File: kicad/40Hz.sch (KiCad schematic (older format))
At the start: 30 parts, among them J1 Power, J2 5V, J3 SSD1306, Q1 IRF540N, SW1 CANC, SW2 UP, SW3 DOWN, SW4 ENT, U1 ESP-12F, U2 WeMos_D1_mini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

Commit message: UPD
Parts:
- SW1: value CANC -> OK
- SW4: value ENT -> CANC
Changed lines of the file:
@@
 P 2200 4950
 F 0 "SW1" H 2200 5235 50  0000 C CNN
-F 1 "CANC" H 2200 5144 50  0000 C CNN
+F 1 "OK" H 2200 5144 50  0000 C CNN
 F 2 "Button_Switch_THT:SW_PUSH_6mm_H5mm" H 2200 5150 50  0001 C CNN
 F 3 "~" H 2200 5150 50  0001 C CNN
@@
 P 2200 6350
 F 0 "SW4" H 2200 6635 50  0000 C CNN
-F 1 "ENT" H 2200 6544 50  0000 C CNN
+F 1 "CANC" H 2200 6544 50  0000 C CNN
 F 2 "Button_Switch_THT:SW_PUSH_6mm_H5mm" H 2200 6550 50  0001 C CNN
 F 3 "~" H 2200 6550 50  0001 C CNN
@@
 	2000 4950 1050 4950
 Text Label 1800 4950 0    50   ~ 0
-IO16
+IO14
 Text Label 1800 5900 0    50   ~ 0
 IO12
@@
 	1300 5400 1300 6400
 Text Label 1800 5400 0    50   ~ 0
-IO14
+IO16
 Wire Wire Line
 	1300 6750 1550 6750

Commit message: Schematics update
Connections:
- wire segments 136 -> 134
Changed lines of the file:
@@
 	1    0    0    -1
 $EndComp
-Wire Wire Line
-	5750 4850 5450 4850
-Wire Wire Line
-	5750 4950 5450 4950
-Text Label 5500 4850 0    50   ~ 0
-ACIN1
-Text Label 5500 4950 0    50   ~ 0
-ACIN2
 Text Label 8550 5350 0    50   ~ 0
 ACIN1

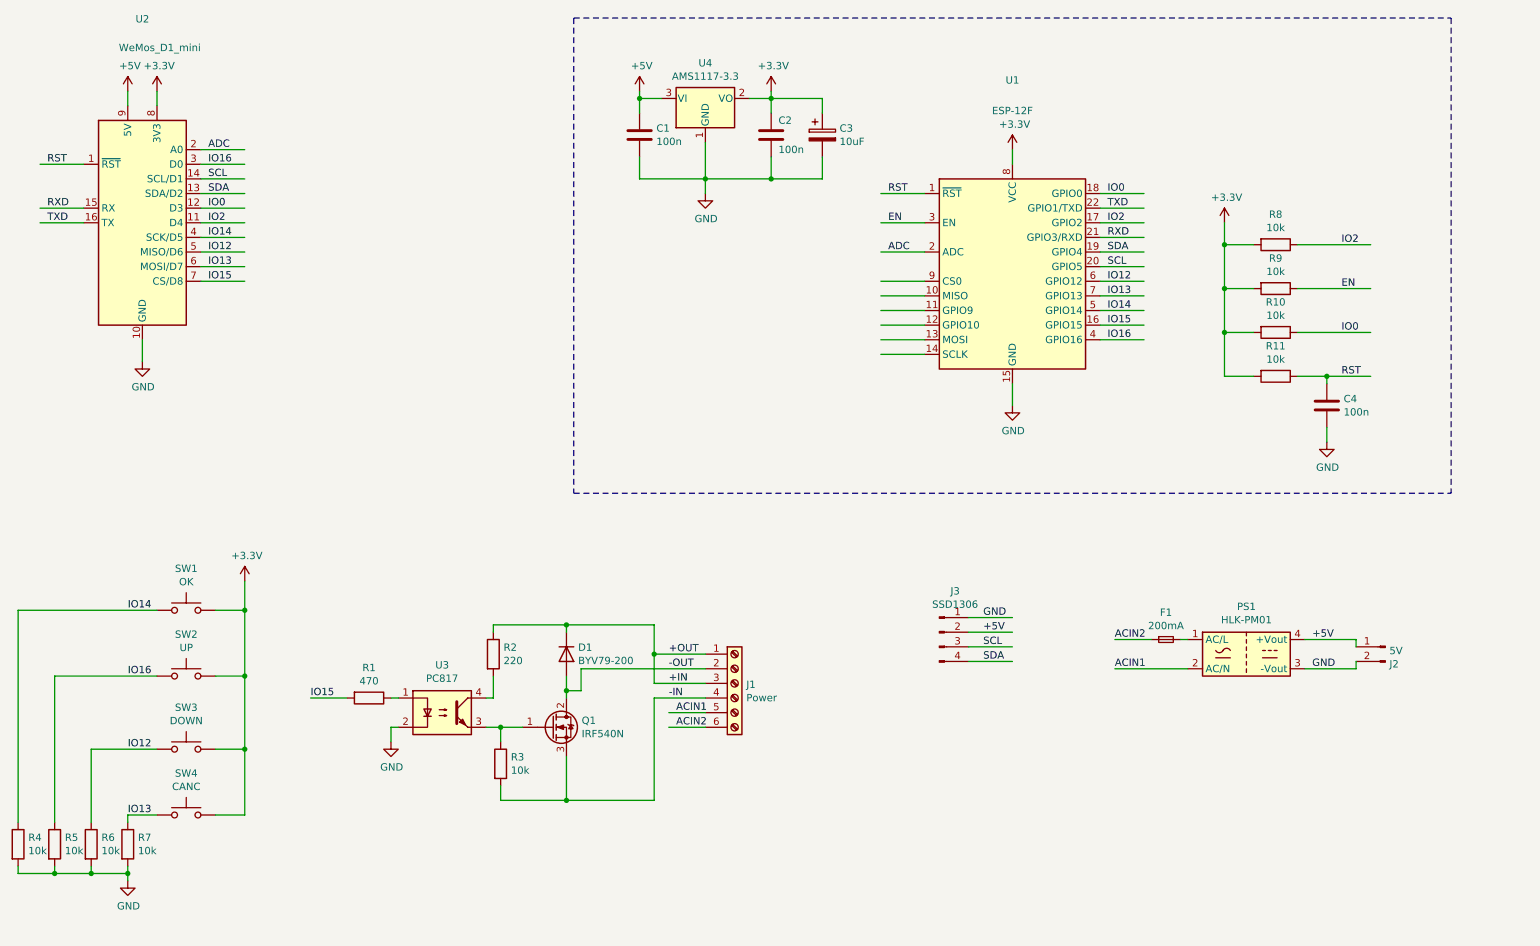
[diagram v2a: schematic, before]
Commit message: Add CRC Check on Settings
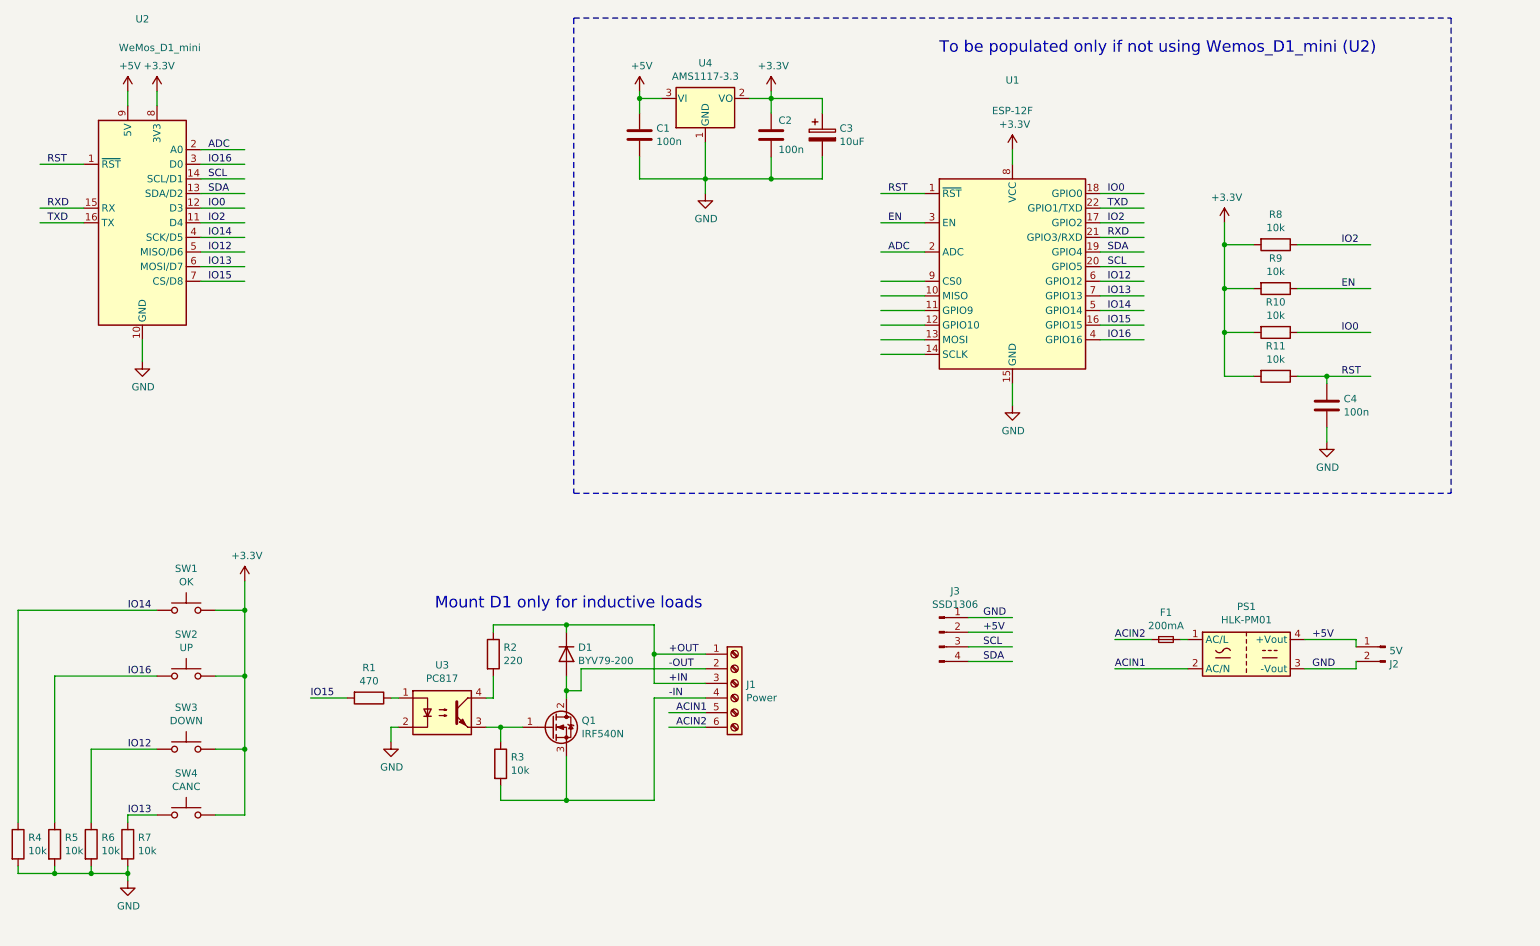
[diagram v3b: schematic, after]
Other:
- note added: "Mount D1 only for inductive loads"
- note added: "To be populated only if not using Wemos_D1_mini (U2)"
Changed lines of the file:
@@
 	4800 6250 4800 5950
 Connection ~ 4800 6250
-$Comp
-L Diode:BYV79-200 D1
-U 1 1 61F3A6D4
-P 4800 5250
-F 0 "D1" V 4754 5330 50  0000 L CNN
-F 1 "BYV79-200" V 4845 5330 50  0000 L CNN
-F 2 "Diode_THT:D_DO-15_P5.08mm_Vertical_KathodeUp" H 4800 5075 50  0001 C CNN
-F 3 "http://pdf.datasheetcatalog.com/datasheet/philips/BYV79-100.pdf" H 4800 5250 50  0001 C CNN
-	1    4800 5250
-	0    1    1    0
-$EndComp
 Connection ~ 4800 5050
 Wire Wire Line
@@
 Text Label 5550 5750 0    50   ~ 0
 ACIN2
+Text Notes 7350 1150 0    79   ~ 0
+To be populated only if not using Wemos_D1_mini (U2)
+$Comp
+L Diode:BYV79-200 D1
+U 1 1 61F3A6D4
+P 4800 5250
+F 0 "D1" V 4754 5330 50  0000 L CNN
+F 1 "BYV79-200" V 4845 5330 50  0000 L CNN
+F 2 "Diode_THT:D_DO-15_P5.08mm_Vertical_KathodeUp" H 4800 5075 50  0001 C CNN
+F 3 "http://pdf.datasheetcatalog.com/datasheet/philips/BYV79-100.pdf" H 4800 5250 50  0001 C CNN
+	1    4800 5250
+	0    1    1    0
+$EndComp
+Text Notes 3900 4950 0    79   ~ 0
+Mount D1 only for inductive loads
 $EndSCHEMATC

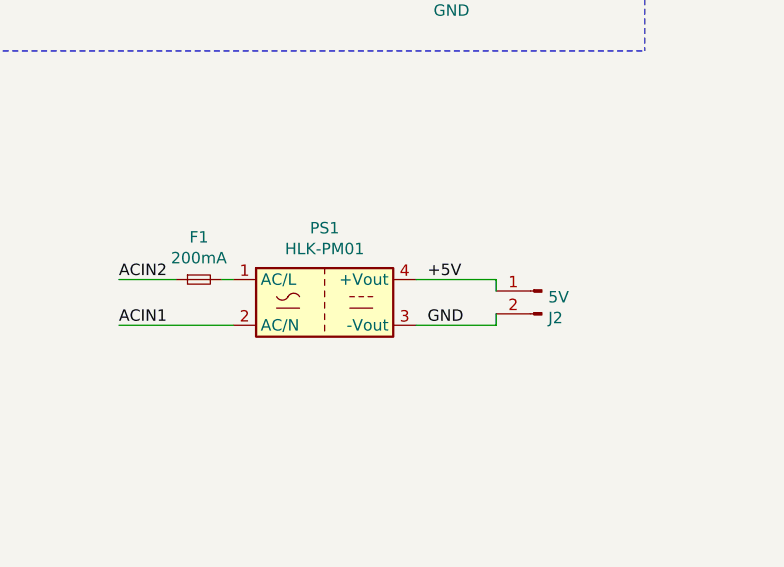
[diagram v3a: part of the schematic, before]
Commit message: Fuse added
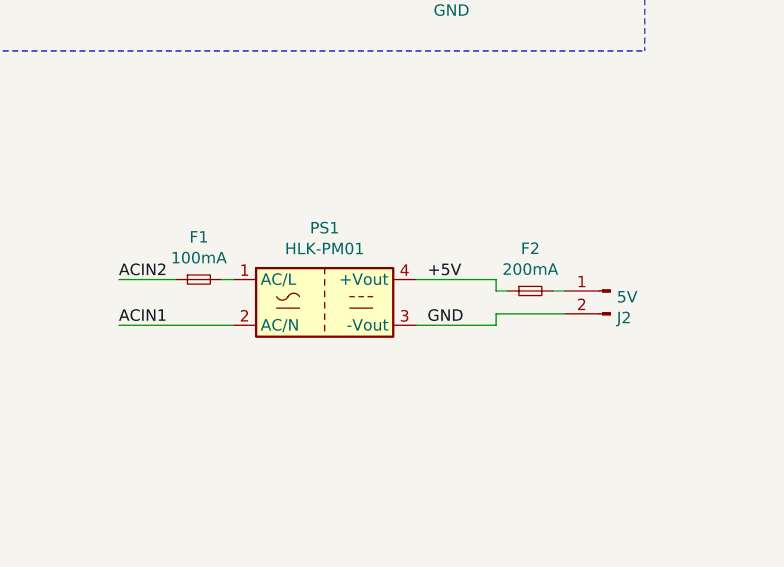
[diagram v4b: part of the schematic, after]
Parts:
- added F2: 200mA, Fuse:Fuse_1206_3216Metric, symbol Device:Fuse_Small
- F1: value 200mA -> 100mA
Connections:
- wire segments 134 -> 137
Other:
- moved on the sheet: J2
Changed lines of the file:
@@
 P 8900 5150
 F 0 "F1" H 8900 5335 50  0000 C CNN
-F 1 "200mA" H 8900 5244 50  0000 C CNN
+F 1 "100mA" H 8900 5244 50  0000 C CNN
 F 2 "Fuse:Fuse_1206_3216Metric" H 8900 5150 50  0001 C CNN
 F 3 "~" H 8900 5150 50  0001 C CNN
@@
 L Connector:Conn_01x02_Male J2
 U 1 1 622AC1D8
-P 10400 5200
-F 0 "J2" H 10372 5082 50  0000 R CNN
-F 1 "5V" H 10372 5173 50  0000 R CNN
-F 2 "TerminalBlock_Phoenix:TerminalBlock_Phoenix_MKDS-3-2-5.08_1x02_P5.08mm_Horizontal" H 10400 5200 50  0001 C CNN
-F 3 "~" H 10400 5200 50  0001 C CNN
-	1    10400 5200
+P 10700 5200
+F 0 "J2" H 10672 5082 50  0000 R CNN
+F 1 "5V" H 10672 5173 50  0000 R CNN
+F 2 "TerminalBlock_Phoenix:TerminalBlock_Phoenix_MKDS-3-2-5.08_1x02_P5.08mm_Horizontal" H 10700 5200 50  0001 C CNN
+F 3 "~" H 10700 5200 50  0001 C CNN
+	1    10700 5200
 	-1   0    0    -1
 $EndComp
@@
 Text Notes 3900 4950 0    79   ~ 0
 Mount D1 only for inductive loads
+$Comp
+L Device:Fuse_Small F2
+U 1 1 621A756A
+P 10350 5200
+F 0 "F2" H 10350 5385 50  0000 C CNN
+F 1 "200mA" H 10350 5294 50  0000 C CNN
+F 2 "Fuse:Fuse_1206_3216Metric" H 10350 5200 50  0001 C CNN
+F 3 "~" H 10350 5200 50  0001 C CNN
+	1    10350 5200
+	1    0    0    -1
+$EndComp
+Wire Wire Line
+	10200 5200 10250 5200
+Wire Wire Line
+	10500 5200 10450 5200
+Wire Wire Line
+	10500 5300 10200 5300
 $EndSCHEMATC

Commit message: Schematic update
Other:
- note added: "Optional AC Power Supply"
- moved on the sheet: F1, F2, J2, J3, PS1, U2
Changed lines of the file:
@@
 	7250 2100 6950 2100
 Wire Wire Line
-	1500 1900 1200 1900
-Wire Wire Line
-	1500 2200 1200 2200
-Wire Wire Line
-	1500 2300 1200 2300
-Wire Wire Line
-	2300 1800 2600 1800
-Wire Wire Line
-	2300 1900 2600 1900
-Wire Wire Line
-	2300 2000 2600 2000
-Wire Wire Line
-	2300 2100 2600 2100
-Wire Wire Line
-	2300 2200 2600 2200
-Wire Wire Line
-	2300 2300 2600 2300
-Wire Wire Line
-	2300 2400 2600 2400
-Wire Wire Line
-	2300 2500 2600 2500
-Wire Wire Line
-	2300 2600 2600 2600
+	2000 2250 1700 2250
+Wire Wire Line
+	2000 2550 1700 2550
+Wire Wire Line
+	2000 2650 1700 2650
+Wire Wire Line
+	2800 2150 3100 2150
+Wire Wire Line
+	2800 2250 3100 2250
+Wire Wire Line
+	2800 2350 3100 2350
+Wire Wire Line
+	2800 2450 3100 2450
+Wire Wire Line
+	2800 2550 3100 2550
+Wire Wire Line
+	2800 2650 3100 2650
+Wire Wire Line
+	2800 2750 3100 2750
+Wire Wire Line
+	2800 2850 3100 2850
+Wire Wire Line
+	2800 2950 3100 2950
 Wire Wire Line
 	7850 3400 7850 3550
 Wire Wire Line
-	1900 3100 1900 3250
+	2400 3450 2400 3600
 $Comp
 L MCU_Module:WeMos_D1_mini U2
 U 1 1 61EF466A
-P 1900 2300
-F 0 "U2" H 1900 3693 50  0000 C CNN
-F 1 "WeMos_D1_mini" H 2019 3497 50  0000 C CNN
-F 2 "Module:WEMOS_D1_mini_light" H 1900 1150 50  0001 C CNN
-F 3 "https://wiki.wemos.cc/products:d1:d1_mini#documentation" H 50  1150 50  0001 C CNN
-	1    1900 2300
+P 2400 2650
+F 0 "U2" H 2400 4043 50  0000 C CNN
+F 1 "WeMos_D1_mini" H 2519 3847 50  0000 C CNN
+F 2 "Module:WEMOS_D1_mini_light" H 2400 1500 50  0001 C CNN
+F 3 "https://wiki.wemos.cc/products:d1:d1_mini#documentation" H 550 1500 50  0001 C CNN
+	1    2400 2650
 	1    0    0    -1
 $EndComp
@@
 L power:GND #PWR0101
 U 1 1 61F05C36
-P 1900 3250
-F 0 "#PWR0101" H 1900 3000 50  0001 C CNN
-F 1 "GND" H 1905 3077 50  0000 C CNN
-F 2 "" H 1900 3250 50  0001 C CNN
-F 3 "" H 1900 3250 50  0001 C CNN
-	1    1900 3250
+P 2400 3600
+F 0 "#PWR0101" H 2400 3350 50  0001 C CNN
+F 1 "GND" H 2405 3427 50  0000 C CNN
+F 2 "" H 2400 3600 50  0001 C CNN
+F 3 "" H 2400 3600 50  0001 C CNN
+	1    2400 3600
 	1    0    0    -1
 $EndComp
@@
 Text Label 7000 2100 0    50   ~ 0
 RST
-Text Label 1250 1900 0    50   ~ 0
+Text Label 1750 2250 0    50   ~ 0
 RST
 Text Label 7000 2500 0    50   ~ 0
 ADC
-Text Label 2350 1800 0    50   ~ 0
+Text Label 2850 2150 0    50   ~ 0
 ADC
 Text Label 8500 2200 0    50   ~ 0
 TXD
-Text Label 1250 2300 0    50   ~ 0
+Text Label 1750 2650 0    50   ~ 0
 TXD
-Text Label 1250 2200 0    50   ~ 0
+Text Label 1750 2550 0    50   ~ 0
 RXD
 Text Label 8500 2400 0    50   ~ 0
@@
 Text Label 8500 3100 0    50   ~ 0
 IO16
-Text Label 2350 1900 0    50   ~ 0
+Text Label 2850 2250 0    50   ~ 0
 IO16
 Text Label 8500 2900 0    50   ~ 0
 IO14
-Text Label 2350 2400 0    50   ~ 0
+Text Label 2850 2750 0    50   ~ 0
 IO14
 Text Label 8500 2700 0    50   ~ 0
 IO12
-Text Label 2350 2500 0    50   ~ 0
+Text Label 2850 2850 0    50   ~ 0
 IO12
 Text Label 8500 2600 0    50   ~ 0
 SCL
-Text Label 2350 2000 0    50   ~ 0
+Text Label 2850 2350 0    50   ~ 0
 SCL
-Text Label 2350 2100 0    50   ~ 0
+Text Label 2850 2450 0    50   ~ 0
 SDA
 Text Label 8500 2500 0    50   ~ 0
@@
 Text Label 8500 2300 0    50   ~ 0
 IO2
-Text Label 2350 2300 0    50   ~ 0
+Text Label 2850 2650 0    50   ~ 0
 IO2
-Text Label 2350 2200 0    50   ~ 0
+Text Label 2850 2550 0    50   ~ 0
 IO0
 Text Label 8500 2100 0    50   ~ 0
@@
 Text Label 8500 2800 0    50   ~ 0
 IO13
-Text Label 2350 2600 0    50   ~ 0
+Text Label 2850 2950 0    50   ~ 0
 IO13
 Text Label 8500 3000 0    50   ~ 0
@@
 L Converter_ACDC:HLK-PM01 PS1
 U 1 1 61F3A82E
-P 9450 5250
-F 0 "PS1" H 9450 5575 50  0000 C CNN
-F 1 "HLK-PM01" H 9450 5484 50  0000 C CNN
-F 2 "Converter_ACDC:Converter_ACDC_HiLink_HLK-PMxx" H 9450 4950 50  0001 C CNN
-F 3 "http://www.hlktech.net/product_detail.php?ProId=54" H 9850 4900 50  0001 C CNN
-	1    9450 5250
-	1    0    0    -1
-$EndComp
-Text Label 9900 5150 0    50   ~ 0
+P 9400 5150
+F 0 "PS1" H 9400 5475 50  0000 C CNN
+F 1 "HLK-PM01" H 9400 5384 50  0000 C CNN
+F 2 "Converter_ACDC:Converter_ACDC_HiLink_HLK-PMxx" H 9400 4850 50  0001 C CNN
+F 3 "http://www.hlktech.net/product_detail.php?ProId=54" H 9800 4800 50  0001 C CNN
+	1    9400 5150
+	1    0    0    -1
+$EndComp
+Text Label 9850 5050 0    50   ~ 0
 +5V
-Text Label 9900 5350 0    50   ~ 0
+Text Label 9850 5250 0    50   ~ 0
 GND
 $Comp
 L Connector:Conn_01x04_Male J3
 U 1 1 61F698E3
-P 7350 5100
-F 0 "J3" H 7458 5381 50  0000 C CNN
-F 1 "SSD1306" H 7458 5290 50  0000 C CNN
-F 2 "Connector_JST:JST_EH_B4B-EH-A_1x04_P2.50mm_Vertical" H 7350 5100 50  0001 C CNN
-F 3 "~" H 7350 5100 50  0001 C CNN
-	1    7350 5100
-	1    0    0    -1
-$EndComp
-Wire Wire Line
-	7550 5000 7850 5000
-Wire Wire Line
-	7550 5100 7850 5100
-Wire Wire Line
-	7550 5200 7850 5200
-Wire Wire Line
-	7550 5300 7850 5300
-Text Label 7650 5000 0    50   ~ 0
+P 6950 5450
+F 0 "J3" H 7058 5731 50  0000 C CNN
+F 1 "SSD1306" H 7058 5640 50  0000 C CNN
+F 2 "Connector_JST:JST_EH_B4B-EH-A_1x04_P2.50mm_Vertical" H 6950 5450 50  0001 C CNN
+F 3 "~" H 6950 5450 50  0001 C CNN
+	1    6950 5450
+	1    0    0    -1
+$EndComp
+Wire Wire Line
+	7150 5350 7450 5350
+Wire Wire Line
+	7150 5450 7450 5450
+Wire Wire Line
+	7150 5550 7450 5550
+Wire Wire Line
+	7150 5650 7450 5650
+Text Label 7250 5350 0    50   ~ 0
 GND
-Text Label 7650 5100 0    50   ~ 0
+Text Label 7250 5450 0    50   ~ 0
 +5V
-Text Label 7650 5200 0    50   ~ 0
+Text Label 7250 5550 0    50   ~ 0
 SCL
-Text Label 7650 5300 0    50   ~ 0
+Text Label 7250 5650 0    50   ~ 0
 SDA
 $Comp
@@
 L power:+3.3V #PWR0107
 U 1 1 6208C6F5
-P 2000 1400
-F 0 "#PWR0107" H 2000 1250 50  0001 C CNN
-F 1 "+3.3V" H 2015 1573 50  0000 C CNN
-F 2 "" H 2000 1400 50  0001 C CNN
-F 3 "" H 2000 1400 50  0001 C CNN
-	1    2000 1400
+P 2500 1750
+F 0 "#PWR0107" H 2500 1600 50  0001 C CNN
+F 1 "+3.3V" H 2515 1923 50  0000 C CNN
+F 2 "" H 2500 1750 50  0001 C CNN
+F 3 "" H 2500 1750 50  0001 C CNN
+	1    2500 1750
 	1    0    0    -1
 $EndComp
@@
 L power:+5V #PWR0108
 U 1 1 6209E392
-P 1800 1400
-F 0 "#PWR0108" H 1800 1250 50  0001 C CNN
-F 1 "+5V" H 1815 1573 50  0000 C CNN
-F 2 "" H 1800 1400 50  0001 C CNN
-F 3 "" H 1800 1400 50  0001 C CNN
-	1    1800 1400
-	1    0    0    -1
-$EndComp
-Wire Wire Line
-	1800 1400 1800 1500
-Wire Wire Line
-	2000 1400 2000 1500
+P 2300 1750
+F 0 "#PWR0108" H 2300 1600 50  0001 C CNN
+F 1 "+5V" H 2315 1923 50  0000 C CNN
+F 2 "" H 2300 1750 50  0001 C CNN
+F 3 "" H 2300 1750 50  0001 C CNN
+	1    2300 1750
+	1    0    0    -1
+$EndComp
+Wire Wire Line
+	2300 1750 2300 1850
+Wire Wire Line
+	2500 1750 2500 1850
 $Comp
 L Device:C C4
@@
 	10000 3350 10300 3350
 Wire Wire Line
-	2300 2700 2600 2700
-Text Label 2350 2700 0    50   ~ 0
+	2800 3050 3100 3050
+Text Label 2850 3050 0    50   ~ 0
 IO15
 Wire Wire Line
@@
 	1    0    0    -1
 $EndComp
-Text Label 8550 5350 0    50   ~ 0
+Text Label 8500 5250 0    50   ~ 0
 ACIN1
 $Comp
 L Device:Fuse_Small F1
 U 1 1 62287233
-P 8900 5150
-F 0 "F1" H 8900 5335 50  0000 C CNN
-F 1 "100mA" H 8900 5244 50  0000 C CNN
-F 2 "Fuse:Fuse_1206_3216Metric" H 8900 5150 50  0001 C CNN
-F 3 "~" H 8900 5150 50  0001 C CNN
-	1    8900 5150
-	1    0    0    -1
-$EndComp
-Wire Wire Line
-	9050 5150 9000 5150
-Wire Wire Line
-	8550 5350 9050 5350
-Wire Wire Line
-	8800 5150 8550 5150
-Text Label 8550 5150 0    50   ~ 0
+P 8850 5050
+F 0 "F1" H 8850 5235 50  0000 C CNN
+F 1 "100mA" H 8850 5144 50  0000 C CNN
+F 2 "Fuse:Fuse_1206_3216Metric" H 8850 5050 50  0001 C CNN
+F 3 "~" H 8850 5050 50  0001 C CNN
+	1    8850 5050
+	1    0    0    -1
+$EndComp
+Wire Wire Line
+	9000 5050 8950 5050
+Wire Wire Line
+	8500 5250 9000 5250
+Wire Wire Line
+	8750 5050 8500 5050
+Text Label 8500 5050 0    50   ~ 0
 ACIN2
 $Comp
 L Connector:Conn_01x02_Male J2
 U 1 1 622AC1D8
-P 10700 5200
-F 0 "J2" H 10672 5082 50  0000 R CNN
-F 1 "5V" H 10672 5173 50  0000 R CNN
-F 2 "TerminalBlock_Phoenix:TerminalBlock_Phoenix_MKDS-3-2-5.08_1x02_P5.08mm_Horizontal" H 10700 5200 50  0001 C CNN
-F 3 "~" H 10700 5200 50  0001 C CNN
-	1    10700 5200
+P 10650 5100
+F 0 "J2" H 10622 4982 50  0000 R CNN
+F 1 "5V" H 10622 5073 50  0000 R CNN
+F 2 "TerminalBlock_Phoenix:TerminalBlock_Phoenix_MKDS-3-2-5.08_1x02_P5.08mm_Horizontal" H 10650 5100 50  0001 C CNN
+F 3 "~" H 10650 5100 50  0001 C CNN
+	1    10650 5100
 	-1   0    0    -1
 $EndComp
 Wire Wire Line
-	10200 5150 10200 5200
-Wire Wire Line
-	9850 5150 10200 5150
-Wire Wire Line
-	10200 5300 10200 5350
-Wire Wire Line
-	9850 5350 10200 5350
+	10150 5050 10150 5100
+Wire Wire Line
+	9800 5050 10150 5050
+Wire Wire Line
+	10150 5200 10150 5250
+Wire Wire Line
+	9800 5250 10150 5250
 $Comp
 L Regulator_Linear:AMS1117-3.3 U4
@@
 	5300 1450 5300 1400
 Connection ~ 6200 1450
-Wire Notes Line
-	10850 900  10850 4150
 Wire Notes Line
 	4850 900  4850 4150
@@
 L Device:Fuse_Small F2
 U 1 1 621A756A
-P 10350 5200
-F 0 "F2" H 10350 5385 50  0000 C CNN
-F 1 "200mA" H 10350 5294 50  0000 C CNN
-F 2 "Fuse:Fuse_1206_3216Metric" H 10350 5200 50  0001 C CNN
-F 3 "~" H 10350 5200 50  0001 C CNN
-	1    10350 5200
-	1    0    0    -1
-$EndComp
-Wire Wire Line
-	10200 5200 10250 5200
-Wire Wire Line
-	10500 5200 10450 5200
-Wire Wire Line
-	10500 5300 10200 5300
+P 10300 5100
+F 0 "F2" H 10300 5285 50  0000 C CNN
+F 1 "200mA" H 10300 5194 50  0000 C CNN
+F 2 "Fuse:Fuse_1206_3216Metric" H 10300 5100 50  0001 C CNN
+F 3 "~" H 10300 5100 50  0001 C CNN
+	1    10300 5100
+	1    0    0    -1
+$EndComp
+Wire Wire Line
+	10150 5100 10200 5100
+Wire Wire Line
+	10450 5100 10400 5100
+Wire Wire Line
+	10450 5200 10150 5200
+Wire Notes Line
+	8350 4150 8350 5750
+Wire Notes Line
+	8350 5750 10850 5750
+Wire Notes Line
+	10850 900  10850 5750
+Text Notes 8750 4650 0    79   ~ 0
+Optional AC Power Supply
 $EndSCHEMATC
